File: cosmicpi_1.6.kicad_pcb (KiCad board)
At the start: 4 copper layers, 128 x 184 mm, 230 parts, among them J1 Barrel_Jack_Switch, J10 Conn_01x02_Female, J11 Conn_01x02_Male, J12 Conn_01x02_Male, J13 Conn_01x02_Female, J14 Conn_01x02_Male, J15 Conn_01x02_Female, J2 SMA, J3 USB_B_Micro, J4 Conn_01x04_Male, J5 Conn_01x04_Male, J6 SWD, J7 Raspberry_Pi_2_3, J8 Conn_01x02_Male, J9 Conn_01x02_Female, Q1 BSS123, Q2 BSS123, U1 MCP47CMB22, U10 TPS62163DSG, U11 LM555, U12 LM555, U13 LP2985-3.3, U14 AD8039, U15 AD8039, U16 LP2985-3.3, U17 MAX1932, U18 MAX1932, U19 AD8039, U2 STM32F401RETx, U3 L76-M33, U4 74HC00, U5 LPS25HB, U6 LM555, U7 LSM9DS1, U8 SI7006-A20, U9 MAX991, Y1 8 MHz

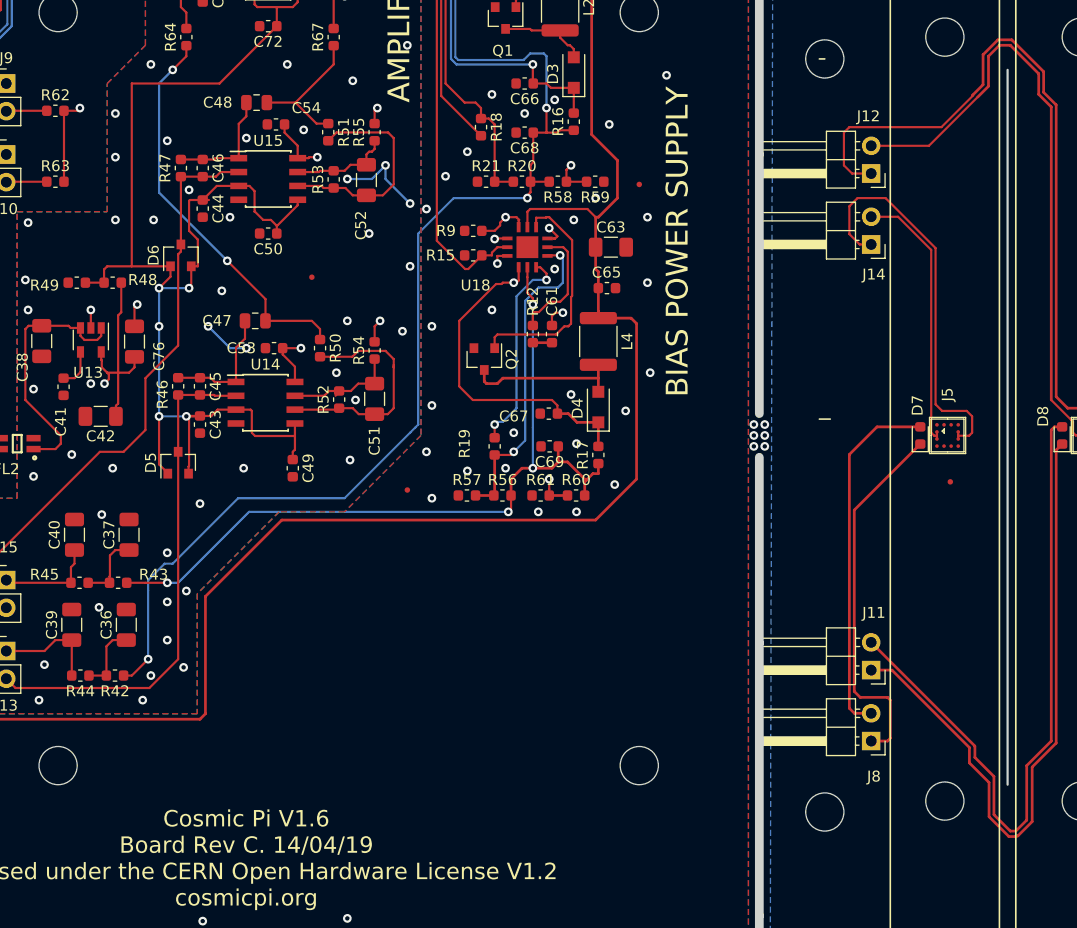
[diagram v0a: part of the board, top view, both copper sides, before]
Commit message: added solder resist on underside
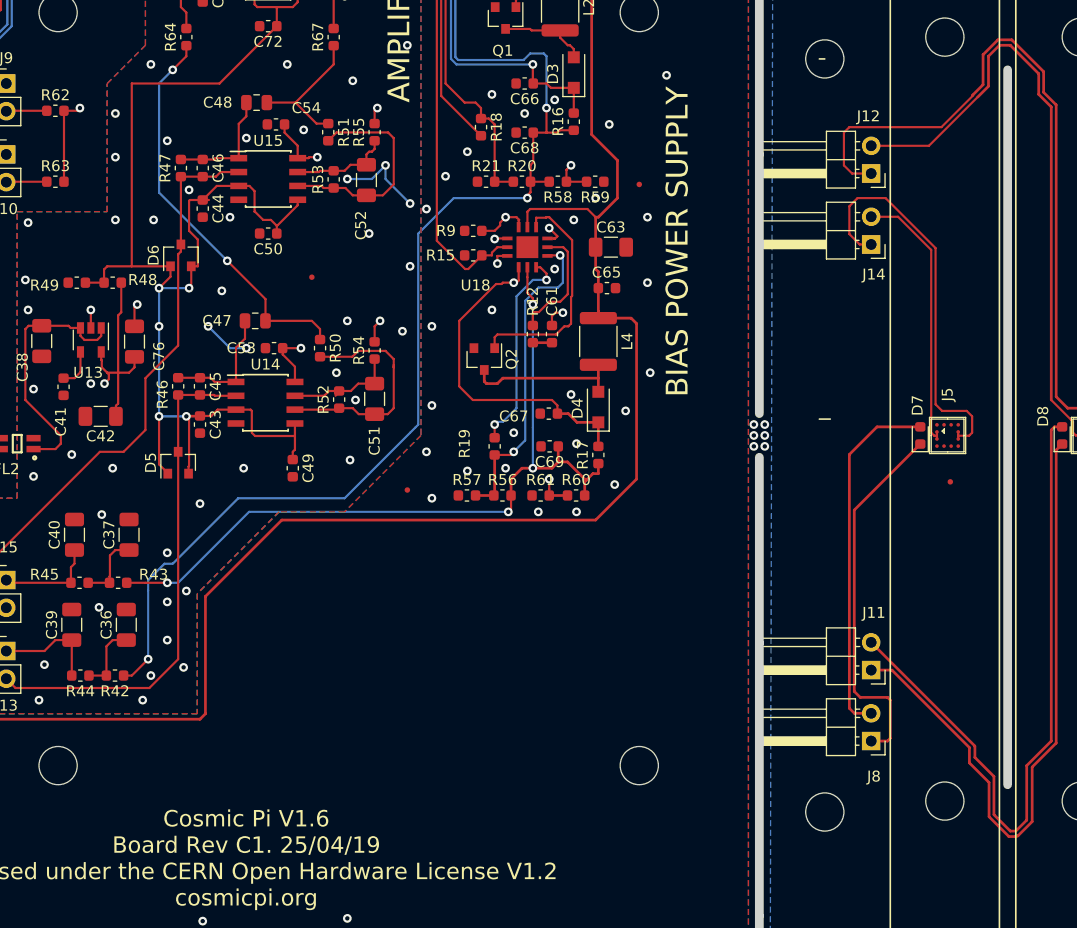
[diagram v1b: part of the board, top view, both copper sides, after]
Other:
- board text added: "Cosmic Pi V1.6 Board Rev C1. 25/04/19 Released under the CERN Open Hardware License V1.2 cosmicpi.org"
- board text removed: "Cosmic Pi V1.6 Board Rev C. 14/04/19 Released under the CERN Open Hardware License V1.2 cosmicpi.org"
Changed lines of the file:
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@@
     (2 In2.Cu signal)
     (31 B.Cu jumper)
-    (33 F.Adhes user hide)
+    (33 F.Adhes user)
+    (34 B.Paste user)
     (35 F.Paste user)
+    (36 B.SilkS user)
     (37 F.SilkS user)
+    (38 B.Mask user)
     (39 F.Mask user)
     (40 Dwgs.User user)
-    (41 Cmts.User user hide)
+    (41 Cmts.User user)
     (42 Eco1.User user)
     (43 Eco2.User user)
@@
     (visible_elements 7FFFFFFF)
     (pcbplotparams
-      (layerselection 0x010aa_ffffffff)
+      (layerselection 0x010fe_ffffffff)
       (usegerberextensions false)
       (usegerberattributes false)
@@
       (drillshape 0)
       (scaleselection 1)
-      (outputdirectory "gerberversion1point6revc/"))
+      (outputdirectory "gerberversion1point6revc1/"))
   )
   (net 0 "")
@@
     (effects (font (size 2 2) (thickness 0.3)))
   )
-  (gr_text "Cosmic Pi V1.6\nBoard Rev C. 14/04/19\nReleased under the CERN Open Hardware License V1.2\ncosmicpi.org" (at 64 153) (layer F.SilkS)
+  (gr_text "Cosmic Pi V1.6\nBoard Rev C1. 25/04/19\nReleased under the CERN Open Hardware License V1.2\ncosmicpi.org" (at 64 153) (layer F.SilkS)
     (effects (font (size 1.5 1.5) (thickness 0.3)))
   )
@@
   (gr_line (start 111 164.25) (end 120.5 164.25) (layer Edge.Cuts) (width 0.8))
   (gr_line (start 144.5 164.25) (end 138.75 164.25) (layer Edge.Cuts) (width 0.8))
-  (gr_line (start 133.75 146.25) (end 133.75 80.75) (layer Edge.Cuts) (width 0.2))
+  (gr_line (start 133.75 146.25) (end 133.75 80.75) (layer Edge.Cuts) (width 0.8))
   (gr_text "Front (0.5mm to inside of front panel)\n" (at 38 15.5) (layer F.Cu)
     (effects (font (size 1.5 1.5) (thickness 0.3)))
